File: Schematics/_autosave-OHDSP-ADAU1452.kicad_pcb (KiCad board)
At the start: 2 copper layers, 100 x 100 mm, 337 parts, among them CN201 COAX, CN401 COAX, CN402 COAX, CN403 COAX, CN404 COAX, CN405 COAX, CN406 COAX, CN407 COAX, CN408 COAX, P201 CONN_2x1, P202 CONN_2x1, P203 CONN_6X2, P204 CONN_6x1, P301 CONN_2x1, P302 CONN_2x1, P303 PIN, P304 PIN, P305 PIN, P306 PIN, P601 CONN_02X05, P602 CONN_02X05, P603 CONN_02X05, P604 CONN_02X05, P605 CONN_3x1, P606 CONN_6X2, P607 CONN_02X05, P608 CONN_02X05, P609 CONN_02X20, P610 CONN_02X05, P611 CONN_5x1, P613 CONN_02X05, P614 CONN_02X05, P615 CONN_02X05, P616 CONN_02X05, SW201 SWITCH, SW202 SWITCH, U201 ADAU1452WBCPZ, U202 ADM13307-5ARZ, U203 25AA1024, U301 IC-REG-XRP7659ISTR-F, U302 IC-REG-XRP7659ISTR-F, U303 XRP6272ITC5TR-F, U304 IC-REG-XC6210B332MR, U305 IC-REG-XC6210B332MR, U401 NB3L553, U402 NB3L553, U501 IC-SPDIF-RX-OPTO, U502 IC-SPDIF-TX-OPTO, X201 24M576

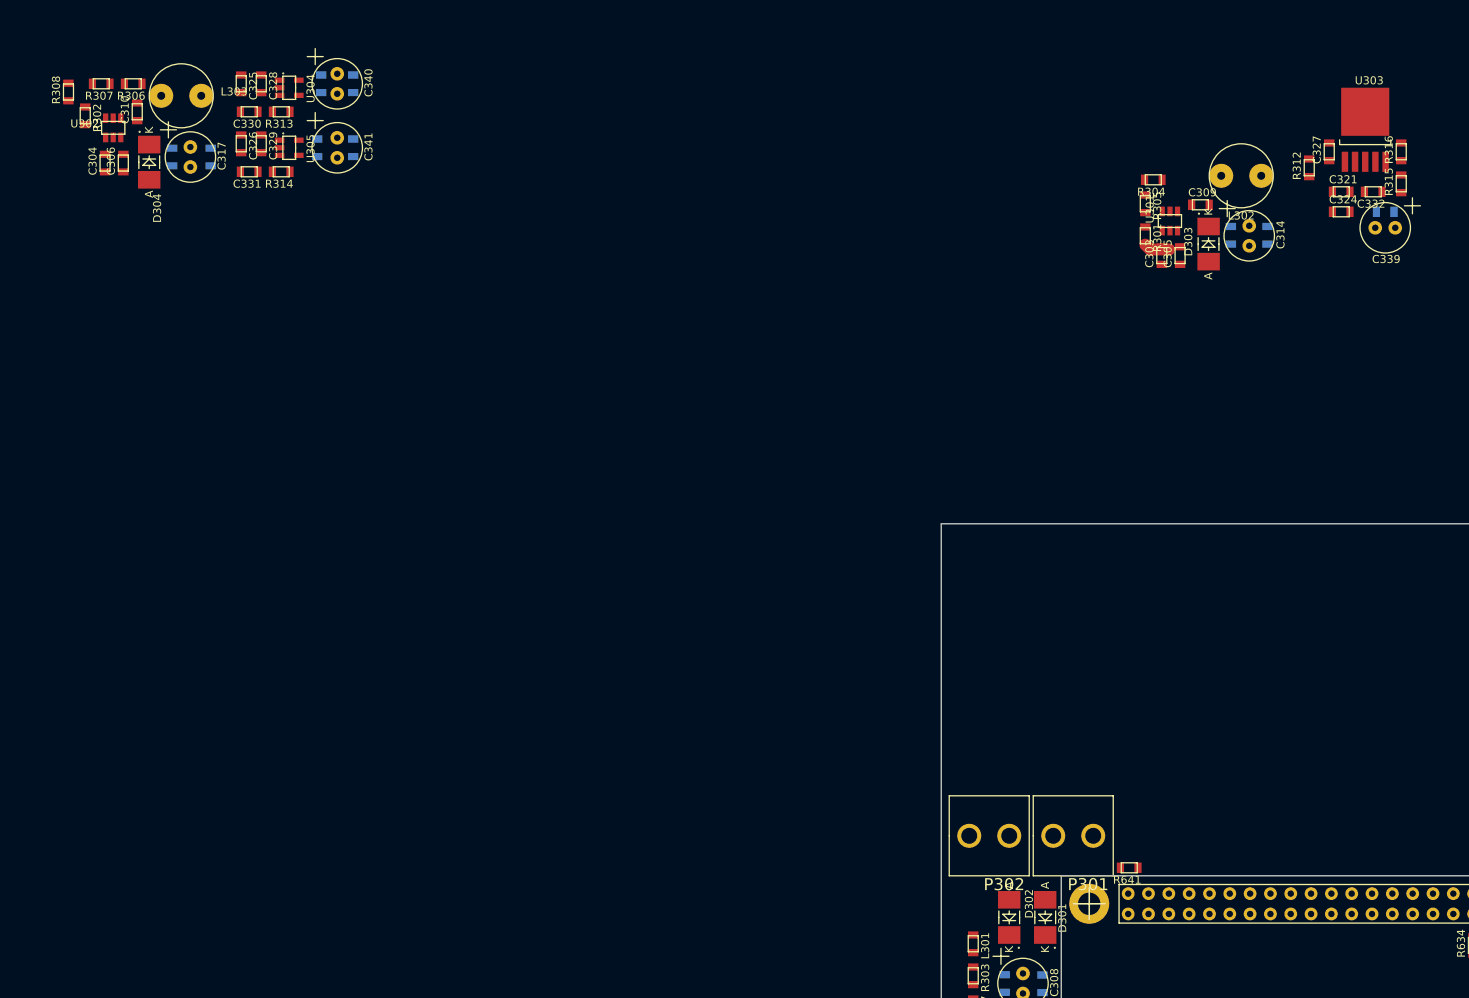
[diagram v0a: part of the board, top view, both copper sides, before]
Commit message: Schematic and PCB changes
Changed and corrected some footprints, removed capacitors, updated
documentation to change 1v5 SMPS to 1v2. Have not removed 1v2 LDO from
schematic yet.
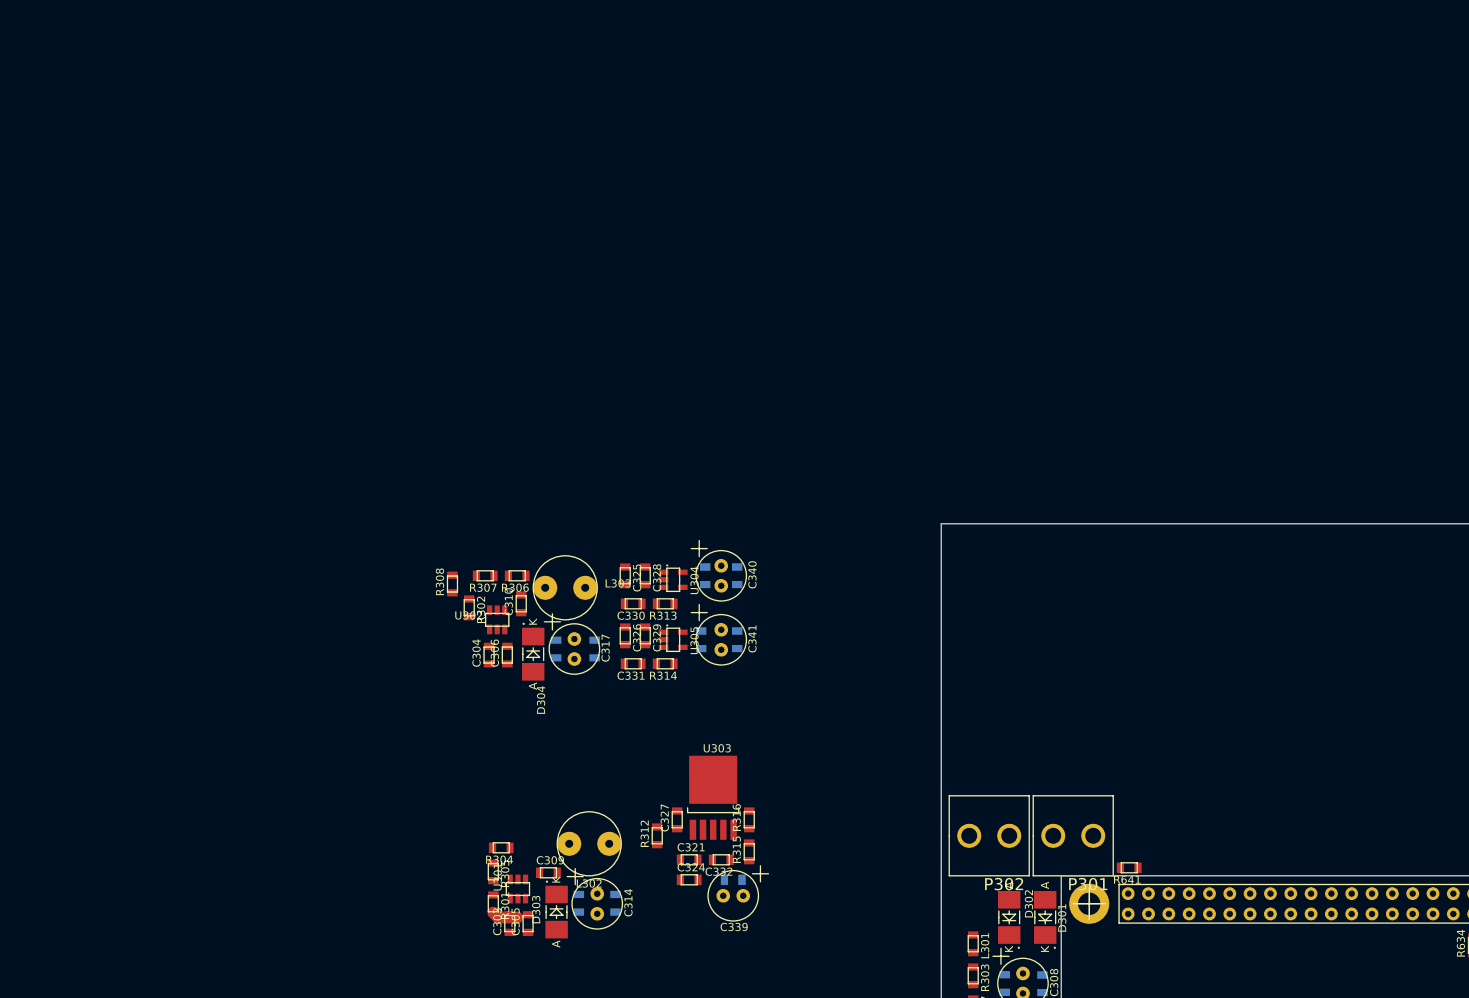
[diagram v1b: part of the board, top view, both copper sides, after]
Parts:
- moved C303 116.7 mm to (151.1, 74.0)
- moved C305 116.7 mm to (153.4, 74.0)
- moved C309 116.7 mm to (155.9, 67.6)
- moved C313 116.7 mm to (164.3, 71.4)
- moved C314 116.7 mm to (162.0, 71.5)
- moved C316 116.7 mm to (159.7, 71.4)
- moved C321 116.7 mm to (173.5, 66.0)
- moved C324 116.7 mm to (173.5, 68.5)
- moved C327 116.7 mm to (172.0, 61.0)
- moved C332 116.7 mm to (177.5, 66.0)
- moved C336 116.7 mm to (179.0, 68.5)
- moved C339 116.7 mm to (179.0, 70.5)
- moved D303 116.7 mm to (156.9, 74.7)
- moved L302 116.7 mm to (161.0, 64.0)
- moved R301 116.7 mm to (149.0, 71.5)
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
